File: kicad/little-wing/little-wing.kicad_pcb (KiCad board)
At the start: 4 copper layers, 14 x 42.1 mm, 68 parts, among them J1 HRO_TYPE-C-31-M-14, J2 Battery, J3 rgb, J4 columns, J5 Conn_01x10, J6 rows, J7 sensor, Q1 AO3401A, Q2 2N7002, SW1 Battery, SW2 Reset, U1 nRF52840_CKAA, U2 nPM1100-CAAx, X1 32MHz, X2 32.768kHz

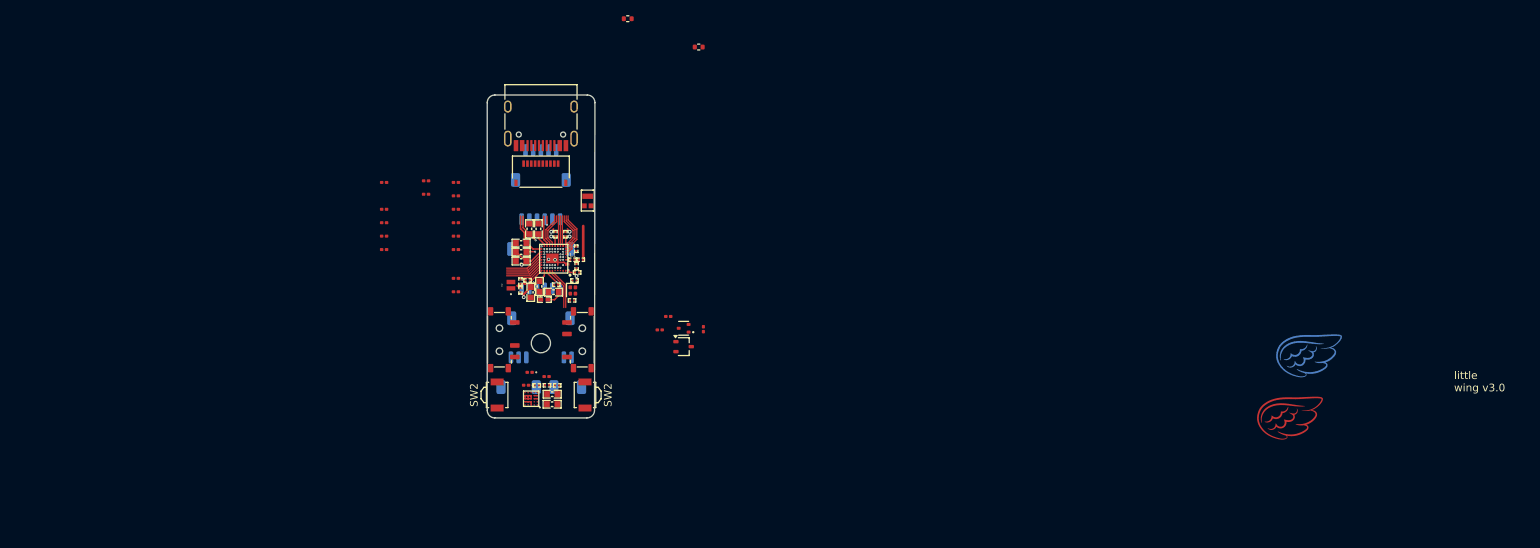
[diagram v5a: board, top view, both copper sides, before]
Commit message: Putting all the components in their rough places
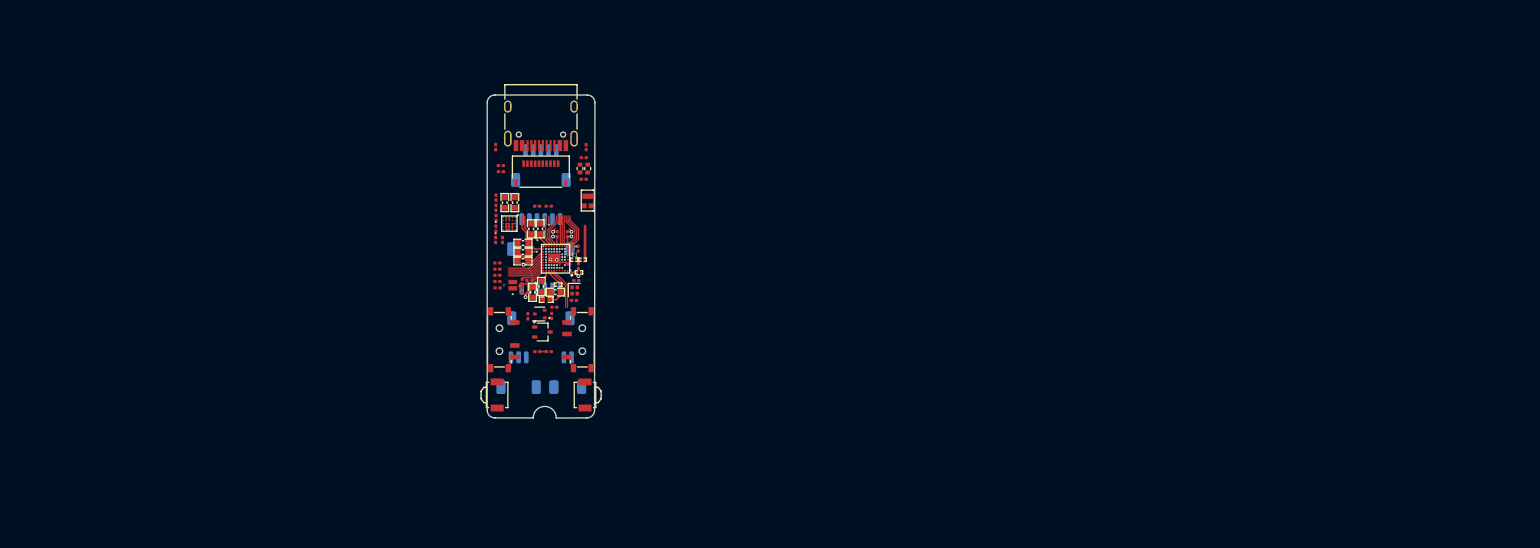
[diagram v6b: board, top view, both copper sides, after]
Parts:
- C1, C17, C18, C2, C3, C5, C7, C8, C9: footprint Capacitors$:CAPC0603X03L_C -> Capacitor_SMD:C_0201_0603Metric
- C22: footprint Parts$:CAPC0603X03L_C -> Capacitor_SMD:C_0201_0603Metric
- R3: footprint RESC0603X03L_C:RESC0603X03L_C -> Resistor_SMD:R_0201_0603Metric
- R_ICHG1: footprint Passive:RESC0603X03L_C -> Resistor_SMD:R_0201_0603Metric
- moved C24 26.7 mm to (146.6, 71.6), turned to -90 degrees
- moved R_DIV1 26.6 mm to (149.6, 91.0)
- moved R_DIV2 26.0 mm to (151.0, 91.0)
- moved C22 25.7 mm to (144.2, 71.0), turned to -90 degrees
- moved C23 25.7 mm to (145.3, 71.6), turned to -90 degrees
- moved R21 24.1 mm to (155.9, 64.4), turned to -90 degrees
- moved R3 24.1 mm to (144.1, 72.3), turned to 90 degrees
- moved U2 23.0 mm to (145.9, 74.4), turned to -90 degrees
- moved R_ICHG1 22.5 mm to (144.2, 73.6), turned to 90 degrees
- moved FB2 21.5 mm to (156.1, 67.2), turned to -90 degrees
- moved LD2 20.8 mm to (144.1, 75.0), turned to -90 degrees
- moved FB1 20.5 mm to (155.1, 67.2), turned to 90 degrees
- moved R8 20.2 mm to (144.3, 82.8), turned to 180 degrees
- moved R18 19.9 mm to (151.4, 86.4)
- moved R22 19.5 mm to (144.1, 64.4), turned to 90 degrees
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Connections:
- AE1 pad 2: (no net) -> GND
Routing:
- net VSENSE: track 7.05 -> 7.89 mm
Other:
- outline, holes or cut-outs redrawn
- board text removed: "little wing v3.0"

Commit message: Backporting footprints from the PCB back to schematic
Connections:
- AE1 pad 2: GND -> (no net)
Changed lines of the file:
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@@
 			(size 0.65 0.6)
 			(layers "F.Cu" "F.Mask" "F.Paste")
-			(net 1 "GND")
 		)
 		(pad "2" smd rect
@@
 			(size 0.7 1.4)
 			(layers "F.Cu" "F.Mask" "F.Paste")
-			(net 1 "GND")
 		)
 		(zone

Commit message: Fixes and space optimisations
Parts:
- moved R8 8.91 mm to (152.8, 85.5), turned to -90 degrees
- moved LD2 3.09 mm to (145.3, 77.9)
- moved R_BLE1 1.77 mm to (143.9, 77.9), turned to -90 degrees
- moved LD3 1.46 mm to (144.6, 77.9)
- moved R11 1.45 mm to (144.4, 81.0)
- moved R14 1.38 mm to (144.4, 81.7)
- moved R15 1.30 mm to (144.4, 82.4)
- moved R16 1.23 mm to (144.4, 83.1)
- moved R_DIV1 0.87 mm to (149.3, 90.2)
- moved R_DIV2 0.86 mm to (150.8, 90.2)
- moved U2 0.69 mm to (145.7, 73.7)
- moved C23 0.54 mm to (145.1, 71.1)
- moved C24 0.54 mm to (146.4, 71.1)
- moved R17 0.44 mm to (152.1, 85.5), turned to -90 degrees
- moved R_ICHG1 0.42 mm to (143.9, 74.0)
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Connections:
- C21 pad 1: VSYS -> VBUS
- C24 pad 2: VSYS -> VBUS
- J1 pad A4: VSYS -> VBUS
- J1 pad A9: VSYS -> VBUS
- J1 pad B4: VSYS -> VBUS
- J1 pad B9: VSYS -> VBUS
- U1 pad G10: unconnected-(U1-P0.12-PadG10) -> BLED
- U1 pad J9: VSYS -> VBUS
- U1 pad K7: BLED -> unconnected-(U1-P0.15-PadK7)
- U2 pad B1: VSYS -> VBUS
- U2 pad B2: VSYS -> VBUS
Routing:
- net VSYS: track 12.3 -> 3.29 mm, vias 2 -> 0
- net unconnected-(U1-P0.12-PadG10): track 5.32 -> 0.00 mm
- net unconnected-(U1-P0.15-PadK7): track 0.00 -> 4.65 mm
- net VBUS: track 0.00 -> 3.49 mm, vias 0 -> 2
- net D+: track 4.10 -> 1.05 mm
- net unconnected-(U1-P0.28/AIN4-PadA6): track 5.54 -> 2.62 mm
- net unconnected-(U1-P0.30/AIN6-PadA7): track 5.59 -> 2.76 mm
- net /Main Module/MCU/RF: track 4.40 -> 7.06 mm
- net GND: track 12.2 -> 14.5 mm
- net VDD: track 17.1 -> 15.4 mm, vias 9 -> 8
- net D-: track 4.27 -> 3.15 mm
- net BLED: track 4.65 -> 5.32 mm
